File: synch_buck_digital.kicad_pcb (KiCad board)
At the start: 4 copper layers, 80 x 80 mm, 48 parts, among them U1 BSC066N06NSATMA1, U2 BSC066N06NSATMA1, U3 INA241A3IDDFR

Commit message: update
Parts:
- moved TP6 178.2 mm to (202.4, 55.7)
- moved TP5 177.3 mm to (205.9, 74.7)
- moved CB1 143.6 mm to (215.6, 70.5)
- moved C_UCC_VDD_HF1 143.6 mm to (213.0, 75.5)
- moved C_UCC_VDD_LF1 143.6 mm to (210.2, 70.5)
- moved J_STM1 130.9 mm to (193.9, 110.4), turned to 90 degrees
- moved C_VFB_FILT1 124.3 mm to (231.2, 89.0)
- moved R1_VFB1 124.3 mm to (231.2, 94.0)
- moved R2_VFB1 124.3 mm to (231.2, 99.0)
- moved D1 124.3 mm to (237.7, 94.5)
- moved C_IN_LF1 109.0 mm to (186.5, 77.8), turned to 90 degrees
- moved C_IN_HF1 99.6 mm to (186.5, 68.5), turned to 90 degrees
- moved C_DT_1U1 96.1 mm to (190.1, 101.0)
- moved R_SHUNT1 92.5 mm to (219.8, 84.1)
- moved R_HYS2 91.4 mm to (184.4, 97.0)
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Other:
- board size 80 x 80 mm -> 60 x 60 mm

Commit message: update
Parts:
- moved TP4 210.0 mm to (235.8, 92.7)
- moved TP1 200.7 mm to (222.7, 100.3)
- moved TP3 192.2 mm to (218.2, 100.3)
- moved TP7 189.5 mm to (219.4, 57.3)
- moved TP2 185.2 mm to (205.8, 78.8)
- moved TP8 176.8 mm to (207.7, 68.0)
- moved C_INA_FILT2 12.0 mm to (217.9, 88.5)
- moved R_FILT_P1 11.9 mm to (219.3, 86.5), turned to -90 degrees
- moved C_INA_FILT3 11.8 mm to (221.9, 88.5), turned to 180 degrees
- moved U_OC1 11.1 mm to (201.3, 100.7)
- moved C_DT_1U1 10.9 mm to (182.9, 92.8), turned to -90 degrees
- moved CB1 10.7 mm to (205.2, 67.8), turned to 90 degrees
- moved C_OUT_HF1 9.73 mm to (231.7, 65.2)
- moved C_OC_10N1 9.40 mm to (205.7, 99.6), turned to 90 degrees
- moved C_IN_LF1 9.26 mm to (185.0, 68.6), turned to -90 degrees
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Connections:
- C_DT_100P1 pad 2: PGND -> SGND
- C_DT_10N1 pad 2: PGND -> SGND
- C_DT_1U1 pad 2: PGND -> SGND
- C_INA_FILT2 pad 1: PGND -> SGND
- C_INA_FILT3 pad 1: PGND -> SGND
- C_INA_VCC1 pad 2: PGND -> SGND
- C_OC_100P1 pad 2: PGND -> SGND
- C_OC_10N1 pad 2: PGND -> SGND
- C_OC_1U1 pad 2: PGND -> SGND
- C_VFB_FILT1 pad 1: PGND -> SGND
- D1 pad 2: PGND -> SGND
- J_STM1 pad 1: /PWM_LS -> /DT_REF
- J_STM1 pad 10: PGND -> SGND
- J_STM1 pad 11: PGND -> SGND
- J_STM1 pad 12: PGND -> SGND
- J_STM1 pad 13: PGND -> SGND
- J_STM1 pad 2: /V_FB -> /COMP_OUT
- J_STM1 pad 3: /DT_REF -> /PROT_OUT
- J_STM1 pad 5: /PROT_OUT -> /PWM_LS
- J_STM1 pad 6: /SENSE_OUT -> /PWM_HS
- J_STM1 pad 7: /PWM_HS -> /SENSE_OUT
- J_STM1 pad 8: /COMP_OUT -> /V_FB
- R1_DT1 pad 2: PGND -> SGND
- R1_VFB1 pad 1: PGND -> SGND
- R_HYS1 pad 1: PGND -> SGND
- R_HYS2 pad 1: PGND -> SGND
- TP1 pad 1: PGND -> SGND
- U3 pad 2: PGND -> SGND
- U3 pad 3: PGND -> SGND
- U3 pad 4: PGND -> SGND
- U3 pad 7: PGND -> SGND
- U_DT1 pad 2: PGND -> SGND
- U_OC1 pad 2: PGND -> SGND
- U_UCC1 pad 7: PGND -> SGND

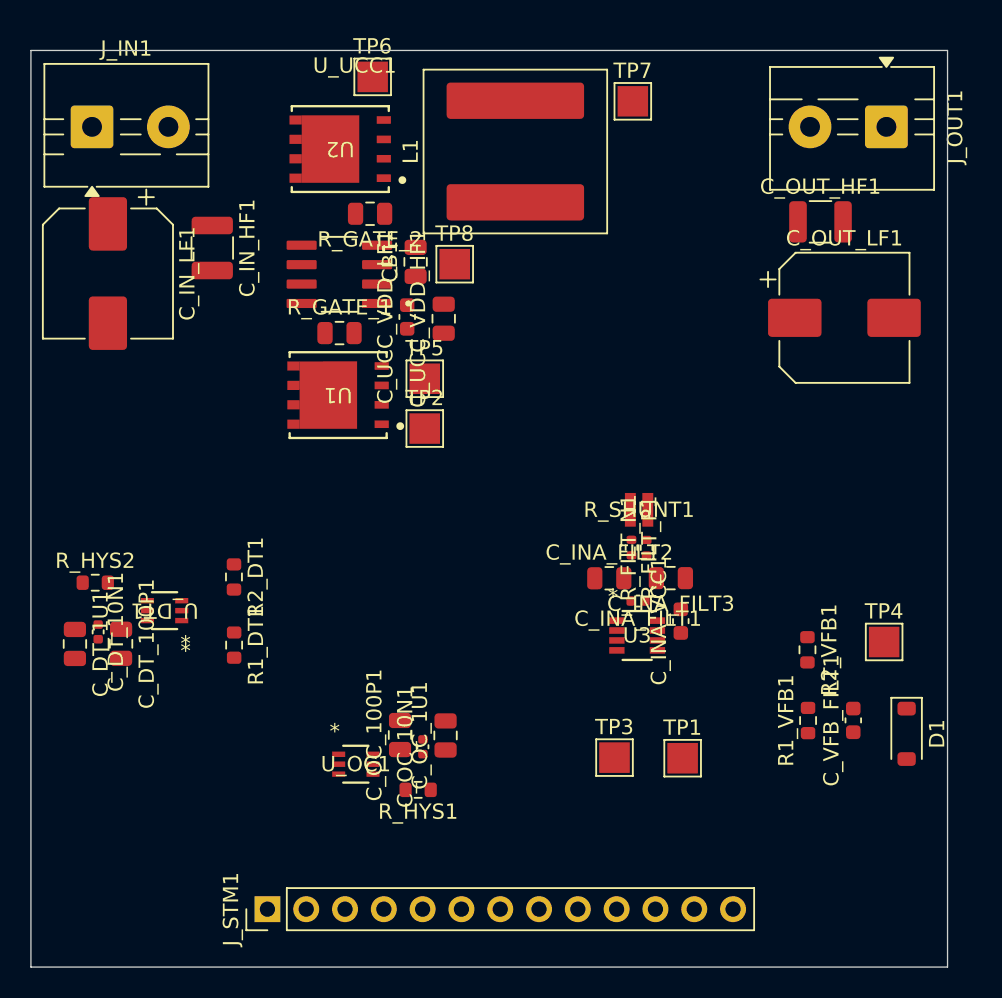
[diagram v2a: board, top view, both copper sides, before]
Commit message: pouring topology started
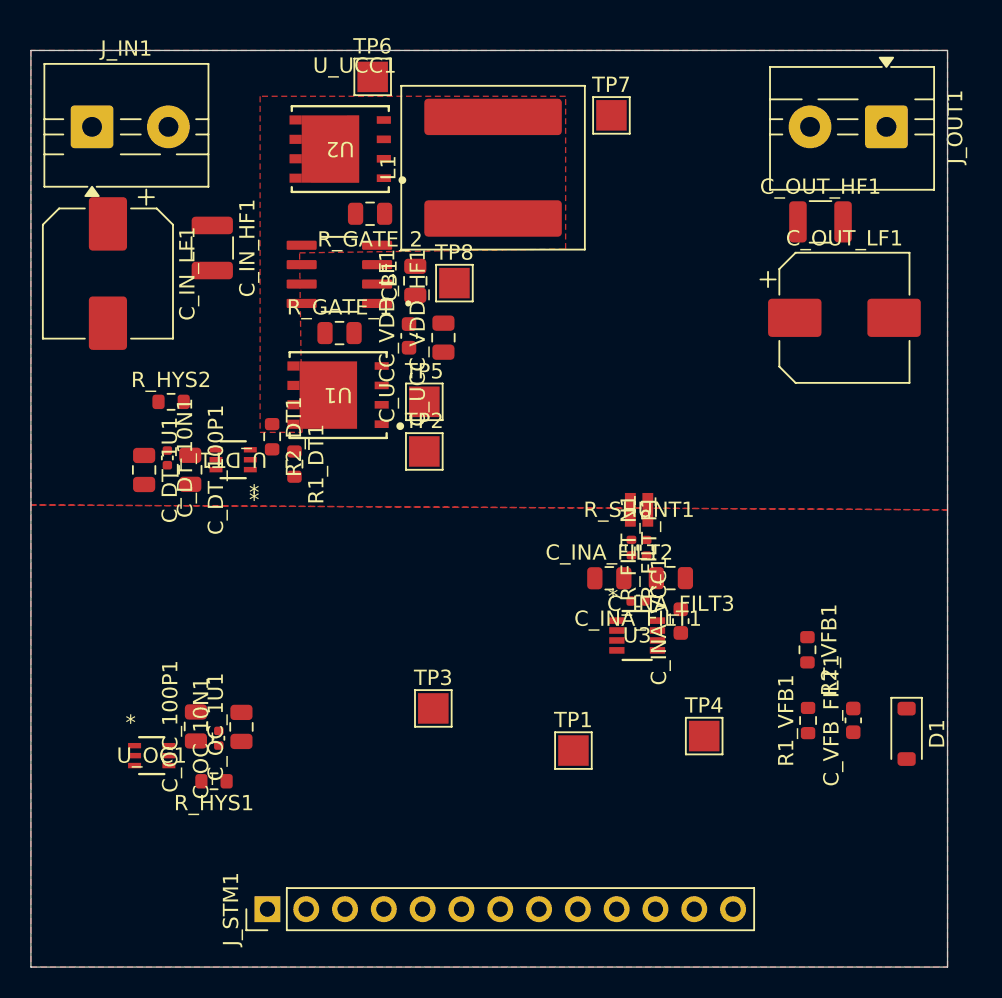
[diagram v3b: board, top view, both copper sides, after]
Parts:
- moved U_OC1 13.4 mm to (187.9, 100.2)
- moved C_OC_100P1 13.4 mm to (190.8, 98.2)
- moved C_OC_10N1 13.4 mm to (192.3, 99.0)
- moved C_OC_1U1 13.4 mm to (193.8, 98.3)
- moved R_HYS1 13.4 mm to (192.0, 101.8)
- moved TP4 13.3 mm to (224.1, 98.9)
- moved R_HYS2 12.8 mm to (189.2, 77.0)
- moved R1_DT1 12.5 mm to (197.2, 81.1)
- moved TP3 12.3 mm to (206.3, 97.1)
- moved C_DT_100P1 12.3 mm to (190.4, 81.5)
- moved C_DT_10N1 12.3 mm to (188.9, 80.7)
- moved C_DT_1U1 12.3 mm to (187.4, 81.5)
- moved U_DT1 10.9 mm to (193.2, 80.8)
- moved R2_DT1 9.51 mm to (195.8, 79.3)
- moved TP1 7.17 mm to (215.5, 99.8)
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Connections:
- R1_DT1 pad 2: SGND -> PGND
- R_HYS2 pad 1: SGND -> PGND
- U_DT1 pad 2: SGND -> PGND
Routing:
- added copper zone on F.Cu, net /SW
- added copper zone on F.Cu, net PGND
- added copper zone on F.Cu, net SGND
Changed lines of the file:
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@@
 		(capping no)
 		(filling no)
+		(zone_defaults)
 		(pcbplotparams
 			(layerselection 0x00000000_00000000_55555555_5755f5ff)
@@
 	(footprint "TestPoint:TestPoint_Pad_2.0x2.0mm"
 		(layer "F.Cu")
-		(at 205.78 78.75)
+		(at 205.75 80.25)
 		(descr "SMD rectangular pad as test Point, square 2.0mm side length")
 		(tags "test point SMD pad rectangle square")
@@
 	(footprint "TLV3603:SC70_DCK_TEX"
 		(layer "F.Cu")
-		(at 201.26755 100.719999)
+		(at 187.90755 100.159999)
 		(tags "TLV3603DCKR-ET ")
 		(property "Reference" "U_OC1"
@@
 	(footprint "TestPoint:TestPoint_Pad_2.0x2.0mm"
 		(layer "F.Cu")
-		(at 207.74 67.99)
+		(at 207.72 69.23)
 		(descr "SMD rectangular pad as test Point, square 2.0mm side length")
 		(tags "test point SMD pad rectangle square")
@@
 	(footprint "Capacitor_SMD:C_0805_2012Metric"
 		(layer "F.Cu")
-		(at 207.14 98.84 90)
+		(at 193.78 98.28 90)
 		(descr "Capacitor SMD 0805 (2012 Metric), square (rectangular) end terminal, IPC-7351 nominal, (Body size source: IPC-SM-782 page 76, https://www.pcb-3d.com/wordpress/wp-content/uploads/ipc-sm-782a_amendment_1_and_2.pdf, https://docs.google.com/spreadsheets/d/1BsfQQcO9C6DZCsRaXUlFlo91Tg2WpOkGARC1WS5S8t0/edit?usp=sharing)")
 		(tags "capacitor")
@@
 	(footprint "Capacitor_SMD:C_0805_2012Metric"
 		(layer "F.Cu")
-		(at 207.02 71.56 90)
+		(at 207 72.8 90)
 		(descr "Capacitor SMD 0805 (2012 Metric), square (rectangular) end terminal, IPC-7351 nominal, (Body size source: IPC-SM-782 page 76, https://www.pcb-3d.com/wordpress/wp-content/uploads/ipc-sm-782a_amendment_1_and_2.pdf, https://docs.google.com/spreadsheets/d/1BsfQQcO9C6DZCsRaXUlFlo91Tg2WpOkGARC1WS5S8t0/edit?usp=sharing)")
 		(tags "capacitor")
@@
 	(footprint "TestPoint:TestPoint_Pad_2.0x2.0mm"
 		(layer "F.Cu")
-		(at 219.4 57.33)
+		(at 218 58.25)
 		(descr "SMD rectangular pad as test Point, square 2.0mm side length")
 		(tags "test point SMD pad rectangle square")
@@
 	(footprint "Capacitor_SMD:C_0402_1005Metric"
 		(layer "F.Cu")
-		(at 205.66 99.58 90)
+		(at 192.3 99.02 90)
 		(descr "Capacitor SMD 0402 (1005 Metric), square (rectangular) end terminal, IPC-7351 nominal, (Body size source: IPC-SM-782 page 76, https://www.pcb-3d.com/wordpress/wp-content/uploads/ipc-sm-782a_amendment_1_and_2.pdf)")
 		(tags "capacitor")
@@
 	(footprint "Resistor_SMD:R_0603_1608Metric"
 		(layer "F.Cu")
-		(at 205.345 102.4 180)
+		(at 191.985 101.84 180)
 		(descr "Resistor SMD 0603 (1608 Metric), square (rectangular) end terminal, IPC-7351 nominal, (Body size source: IPC-SM-782 page 72, https://www.pcb-3d.com/wordpress/wp-content/uploads/ipc-sm-782a_amendment_1_and_2.pdf)")
 		(tags "resistor")
@@
 	(footprint "TLV3603:SC70_DCK_TEX"
 		(layer "F.Cu")
-		(at 188.74755 90.669999 180)
+		(at 193.23605 80.789999 180)
 		(tags "TLV3603DCKR-ET ")
 		(property "Reference" "U_DT1"
@@
 			(size 0.8509 0.3556)
 			(layers "F.Cu" "F.Mask" "F.Paste")
-			(net "SGND")
+			(net "PGND")
 			(pinfunction "VEE_2")
 			(pintype "power_in")
@@
 	(footprint "Capacitor_SMD:C_0402_1005Metric"
 		(layer "F.Cu")
-		(at 184.4 92.06 -90)
+		(at 188.93 80.67 -90)
 		(descr "Capacitor SMD 0402 (1005 Metric), square (rectangular) end terminal, IPC-7351 nominal, (Body size source: IPC-SM-782 page 76, https://www.pcb-3d.com/wordpress/wp-content/uploads/ipc-sm-782a_amendment_1_and_2.pdf)")
 		(tags "capacitor")
@@
 	(footprint "Capacitor_SMD:C_0805_2012Metric"
 		(layer "F.Cu")
-		(at 204.16 98.81 90)
+		(at 190.8 98.25 90)
 		(descr "Capacitor SMD 0805 (2012 Metric), square (rectangular) end terminal, IPC-7351 nominal, (Body size source: IPC-SM-782 page 76, https://www.pcb-3d.com/wordpress/wp-content/uploads/ipc-sm-782a_amendment_1_and_2.pdf, https://docs.google.com/spreadsheets/d/1BsfQQcO9C6DZCsRaXUlFlo91Tg2WpOkGARC1WS5S8t0/edit?usp=sharing)")
 		(tags "capacitor")
@@
 	(footprint "Resistor_SMD:R_0603_1608Metric"
 		(layer "F.Cu")
-		(at 184.21 88.84)
+		(at 189.175 77)
 		(descr "Resistor SMD 0603 (1608 Metric), square (rectangular) end terminal, IPC-7351 nominal, (Body size source: IPC-SM-782 page 72, https://www.pcb-3d.com/wordpress/wp-content/uploads/ipc-sm-782a_amendment_1_and_2.pdf)")
 		(tags "resistor")
@@
 			(layers "F.Cu" "F.Mask" "F.Paste")
 			(roundrect_rratio 0.25)
-			(net "SGND")
+			(net "PGND")
 			(pintype "passive")
 		)
@@
 	(footprint "Capacitor_SMD:C_0805_2012Metric"
 		(layer "F.Cu")
-		(at 185.9 92.84 -90)
+		(at 190.43 81.45 -90)
 		(descr "Capacitor SMD 0805 (2012 Metric), square (rectangular) end terminal, IPC-7351 nominal, (Body size source: IPC-SM-782 page 76, https://www.pcb-3d.com/wordpress/wp-content/uploads/ipc-sm-782a_amendment_1_and_2.pdf, https://docs.google.com/spreadsheets/d/1BsfQQcO9C6DZCsRaXUlFlo91Tg2WpOkGARC1WS5S8t0/edit?usp=sharing)")
 		(tags "capacitor")
@@
 	(footprint "TestPoint:TestPoint_Pad_2.0x2.0mm"
 		(layer "F.Cu")
-		(at 222.66 100.33)
+		(at 215.51 99.83)
 		(descr "SMD rectangular pad as test Point, square 2.0mm side length")
 		(tags "test point SMD pad rectangle square")
@@
 	(footprint "Capacitor_SMD:C_0603_1608Metric"
 		(layer "F.Cu")
-		(at 204.63 71.445 90)
+		(at 204.75 72.685 90)
 		(descr "Capacitor SMD 0603 (1608 Metric), square (rectangular) end terminal, IPC-7351 nominal, (Body size source: IPC-SM-782 page 76, https://www.pcb-3d.com/wordpress/wp-content/uploads/ipc-sm-782a_amendment_1_and_2.pdf)")
 		(tags "capacitor")
@@
 	(footprint "Capacitor_SMD:C_0805_2012Metric"
 		(layer "F.Cu")
-		(at 205.18 67.84 90)
+		(at 205.16 69.08 90)
 		(descr "Capacitor SMD 0805 (2012 Metric), square (rectangular) end terminal, IPC-7351 nominal, (Body size source: IPC-SM-782 page 76, https://www.pcb-3d.com/wordpress/wp-content/uploads/ipc-sm-782a_amendment_1_and_2.pdf, https://docs.google.com/spreadsheets/d/1BsfQQcO9C6DZCsRaXUlFlo91Tg2WpOkGARC1WS5S8t0/edit?usp=sharing)")
 		(tags "capacitor")
@@
 	(footprint "Resistor_SMD:R_0603_1608Metric"
 		(layer "F.Cu")
-		(at 193.29 88.465 -90)
+		(at 195.79 79.285 -90)
 		(descr "Resistor SMD 0603 (1608 Metric), square (rectangular) end terminal, IPC-7351 nominal, (Body size source: IPC-SM-782 page 72, https://www.pcb-3d.com/wordpress/wp-content/uploads/ipc-sm-782a_amendment_1_and_2.pdf)")
 		(tags "resistor")
@@
 	(footprint "TestPoint:TestPoint_Pad_2.0x2.0mm"
 		(layer "F.Cu")
-		(at 235.85 92.72)
+		(at 224.07 98.88)
 		(descr "SMD rectangular pad as test Point, square 2.0mm side length")
 		(tags "test point SMD pad rectangle square")
@@
 	(footprint "Capacitor_SMD:C_0805_2012Metric"
 		(layer "F.Cu")
-		(at 182.88 92.85 -90)
+		(at 187.41 81.46 -90)
 		(descr "Capacitor SMD 0805 (2012 Metric), square (rectangular) end terminal, IPC-7351 nominal, (Body size source: IPC-SM-782 page 76, https://www.pcb-3d.com/wordpress/wp-content/uploads/ipc-sm-782a_amendment_1_and_2.pdf, https://docs.google.com/spreadsheets/d/1BsfQQcO9C6DZCsRaXUlFlo91Tg2WpOkGARC1WS5S8t0/edit?usp=sharing)")
 		(tags "capacitor")
@@
 	(footprint "Resistor_SMD:R_0603_1608Metric"
 		(layer "F.Cu")
-		(at 193.3 92.925 -90)
+		(at 197.25 81.075 -90)
 		(descr "Resistor SMD 0603 (1608 Metric), square (rectangular) end terminal, IPC-7351 nominal, (Body size source: IPC-SM-782 page 72, https://www.pcb-3d.com/wordpress/wp-content/uploads/ipc-sm-782a_amendment_1_and_2.pdf)")
 		(tags "resistor")
@@
 			(layers "F.Cu" "F.Mask" "F.Paste")
 			(roundrect_rratio 0.25)
-			(net "SGND")
+			(net "PGND")
 			(pintype "passive")
 		)
@@
 	(footprint "Inductor_SMD:L_Coilcraft_XAL1010-XXX"
 		(layer "F.Cu")
-		(at 211.71 60.615 90)
+		(at 210.25 61.675 90)
 		(descr "Inductor, Coilcraft, XAL1010-XXX, 10.5x11.8x10.0mm, (https://www.coilcraft.com/getmedia/dd74e670-e705-456a-9a69-585fe02eaf3c/xal1010.pdf)")
 		(tags "xal")
@@
 	(footprint "TestPoint:TestPoint_Pad_2.0x2.0mm"
 		(layer "F.Cu")
-		(at 218.2 100.29)
+		(at 206.34 97.07)
 		(descr "SMD rectangular pad as test Point, square 2.0mm side length")
 		(tags "test point SMD pad rectangle square")
@@
 	(footprint "TestPoint:TestPoint_Pad_2.0x2.0mm"
 		(layer "F.Cu")
-		(at 205.78 75.49)
+		(at 205.75 77)
 		(descr "SMD rectangular pad as test Point, square 2.0mm side length")
 		(tags "test point SMD pad rectangle square")
@@
 		(layer "Edge.Cuts")
 	)
+	(zone
+		(net "/SW")
+		(layer "F.Cu")
+		(name "SW")
+		(hatch edge 0.5)
+		(priority 2)
+		(connect_pads yes
+			(clearance 0.5)
+		)
+		(min_thickness 0.25)
+		(fill
+			(thermal_gap 0.5)
+			(thermal_bridge_width 0.5)
+			(island_removal_mode 0)
+		)
+		(polygon
+			(pts
+				(xy 195 79) (xy 197.75 79) (xy 197.585498 67.25) (xy 215 67) (xy 215 57) (xy 195 57)
+			)
+		)
+	)
+	(zone
+		(net "SGND")
+		(layer "F.Cu")
+		(name "SGND")
+		(hatch edge 0.5)
+		(priority 1)
+		(connect_pads yes
+			(clearance 0.5)
+		)
+		(min_thickness 0.25)
+		(fill yes
+			(thermal_gap 0.5)
+			(thermal_bridge_width 0.5)
+			(island_removal_mode 0)
+		)
+		(polygon
+			(pts
+				(xy 180 83.75) (xy 180 114) (xy 240 114) (xy 240 84.07)
+			)
+		)
+	)
+	(zone
+		(net "PGND")
+		(layer "F.Cu")
+		(name "PGND")
+		(hatch edge 0.5)
+		(connect_pads yes
+			(clearance 0.5)
+		)
+		(min_thickness 0.25)
+		(fill yes
+			(thermal_gap 0.5)
+			(thermal_bridge_width 0.5)
+			(island_removal_mode 0)
+		)
+		(polygon
+			(pts
+				(xy 240 84.07) (xy 240 54) (xy 180 54) (xy 180 83.75)
+			)
+		)
+	)
 	(embedded_fonts no)

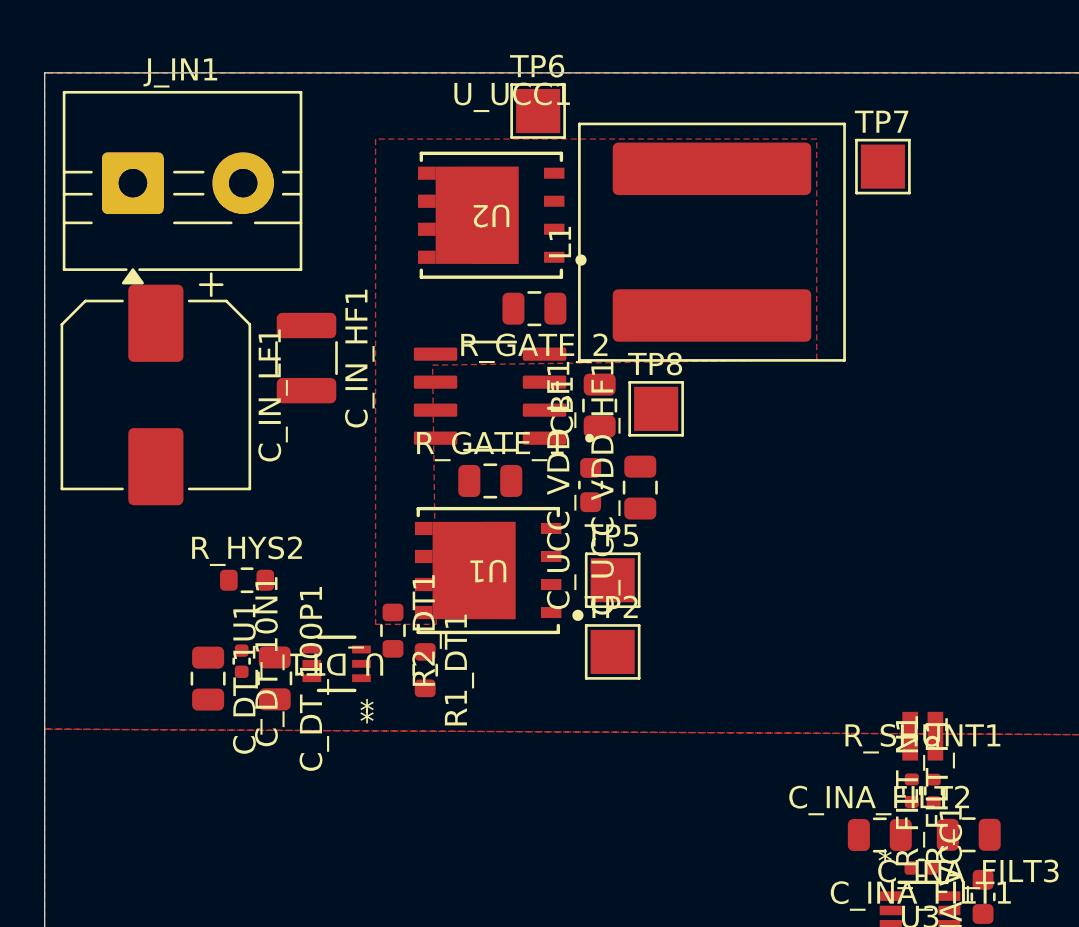
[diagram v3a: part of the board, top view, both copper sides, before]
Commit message: Smaller SW Pour
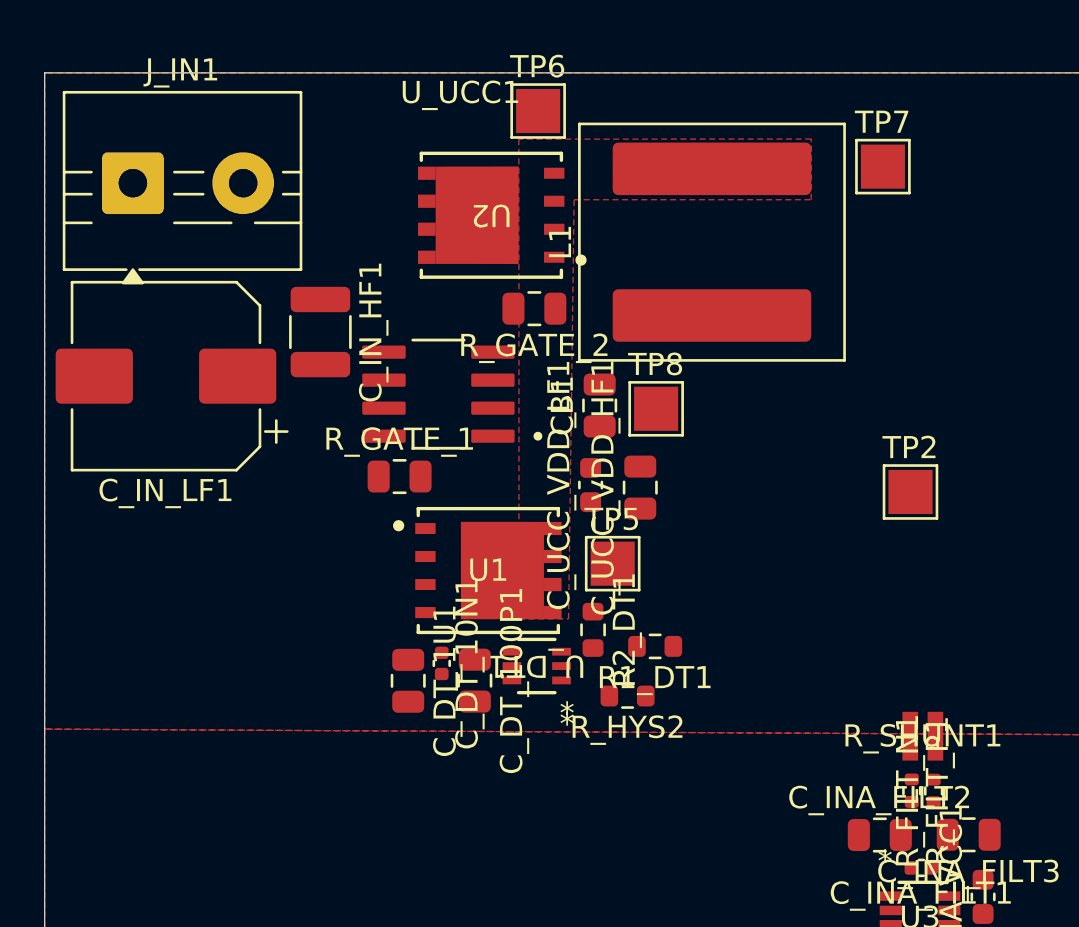
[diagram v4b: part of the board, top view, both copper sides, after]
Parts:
- moved R_HYS2 18.0 mm to (206.4, 82.2), turned to 180 degrees
- moved TP2 15.3 mm to (219.2, 73.0)
- moved R1_DT1 10.5 mm to (207.7, 80.0), turned to 180 degrees
- moved C_DT_100P1 9.07 mm to (199.5, 81.5)
- moved C_DT_10N1 9.07 mm to (198.0, 80.8)
- moved C_DT_1U1 9.07 mm to (196.5, 81.6)
- moved U_DT1 9.07 mm to (202.3, 80.9)
- moved R2_DT1 9.07 mm to (204.9, 79.2)
- moved R_GATE_1 4.11 mm to (196.1, 72.3)
- moved U_UCC1 2.34 mm to (197.8, 68.6)
- moved C_IN_HF1 1.34 mm to (192.5, 65.8)
- moved C_IN_LF1 0.97 mm to (185.5, 67.8), turned to 180 degrees
- moved TP5 0.75 mm to (205.8, 76.2)
- turned U1 to 0 degrees
